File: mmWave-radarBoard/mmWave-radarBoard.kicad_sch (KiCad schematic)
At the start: 1 part, among them U2 XI6432BRQAAMY

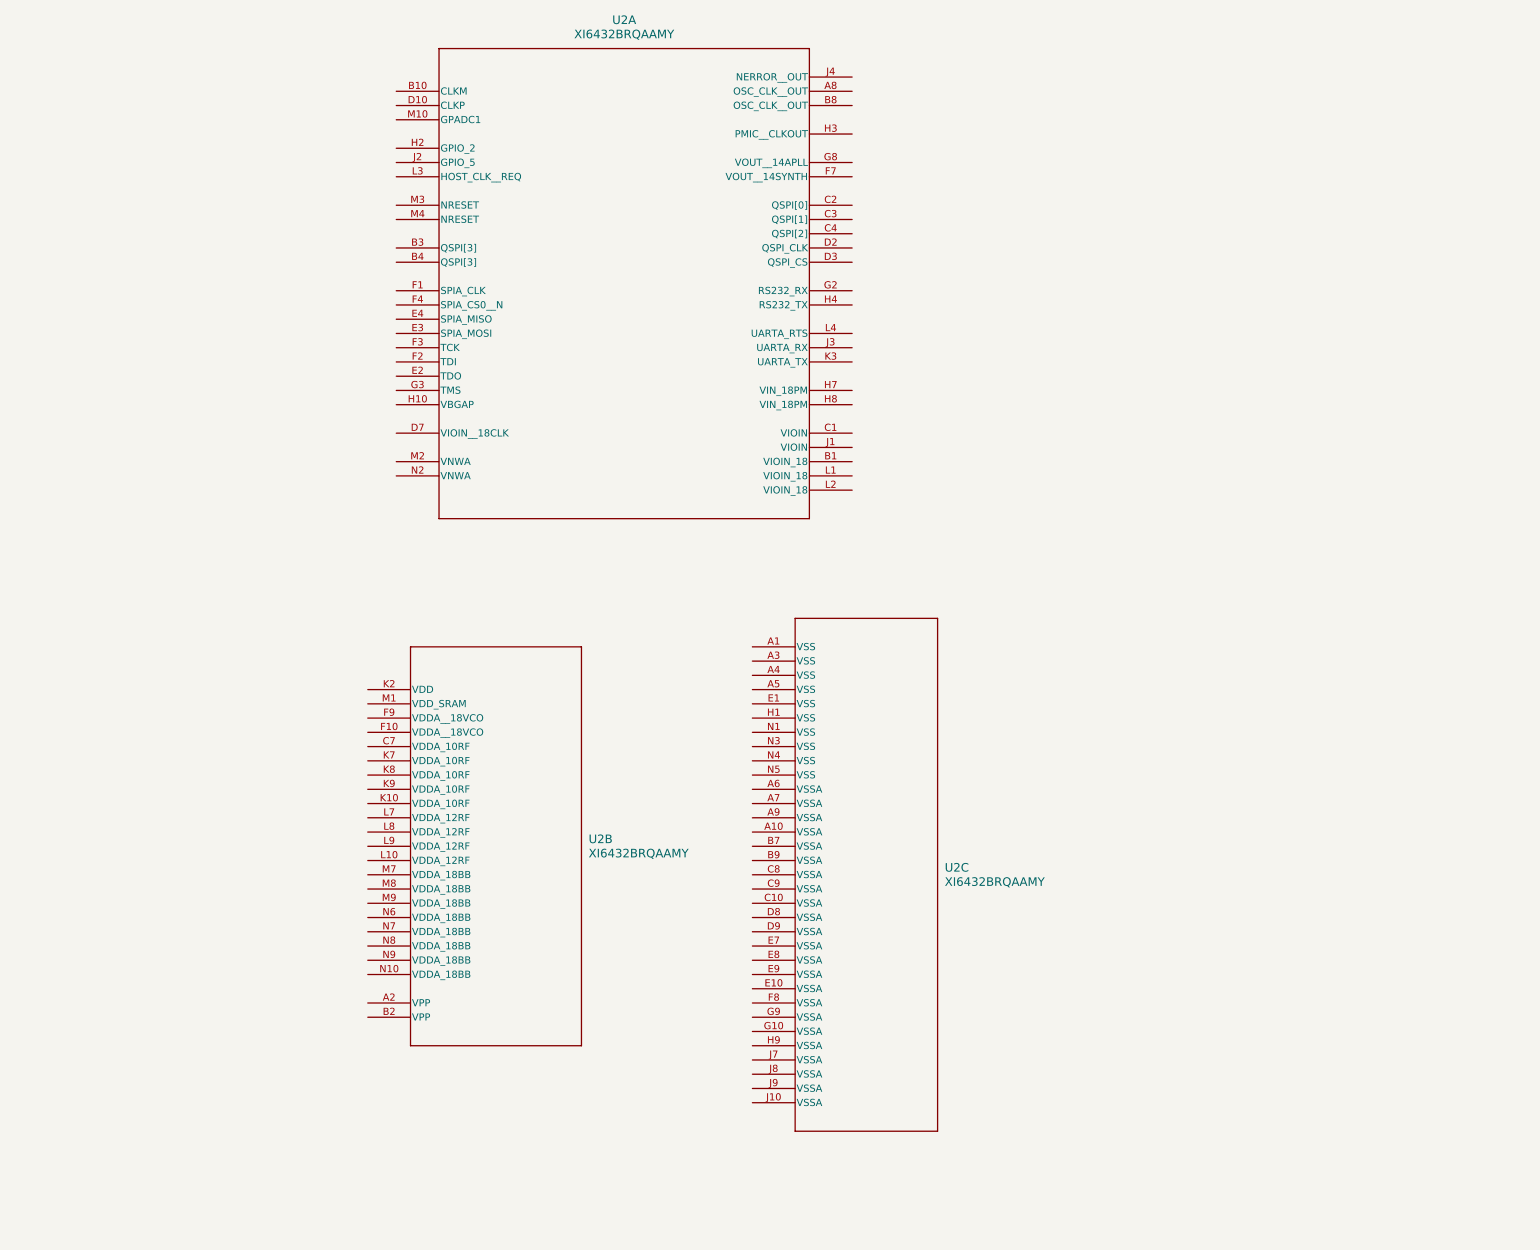
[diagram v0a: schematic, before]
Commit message: Started working on the schematic
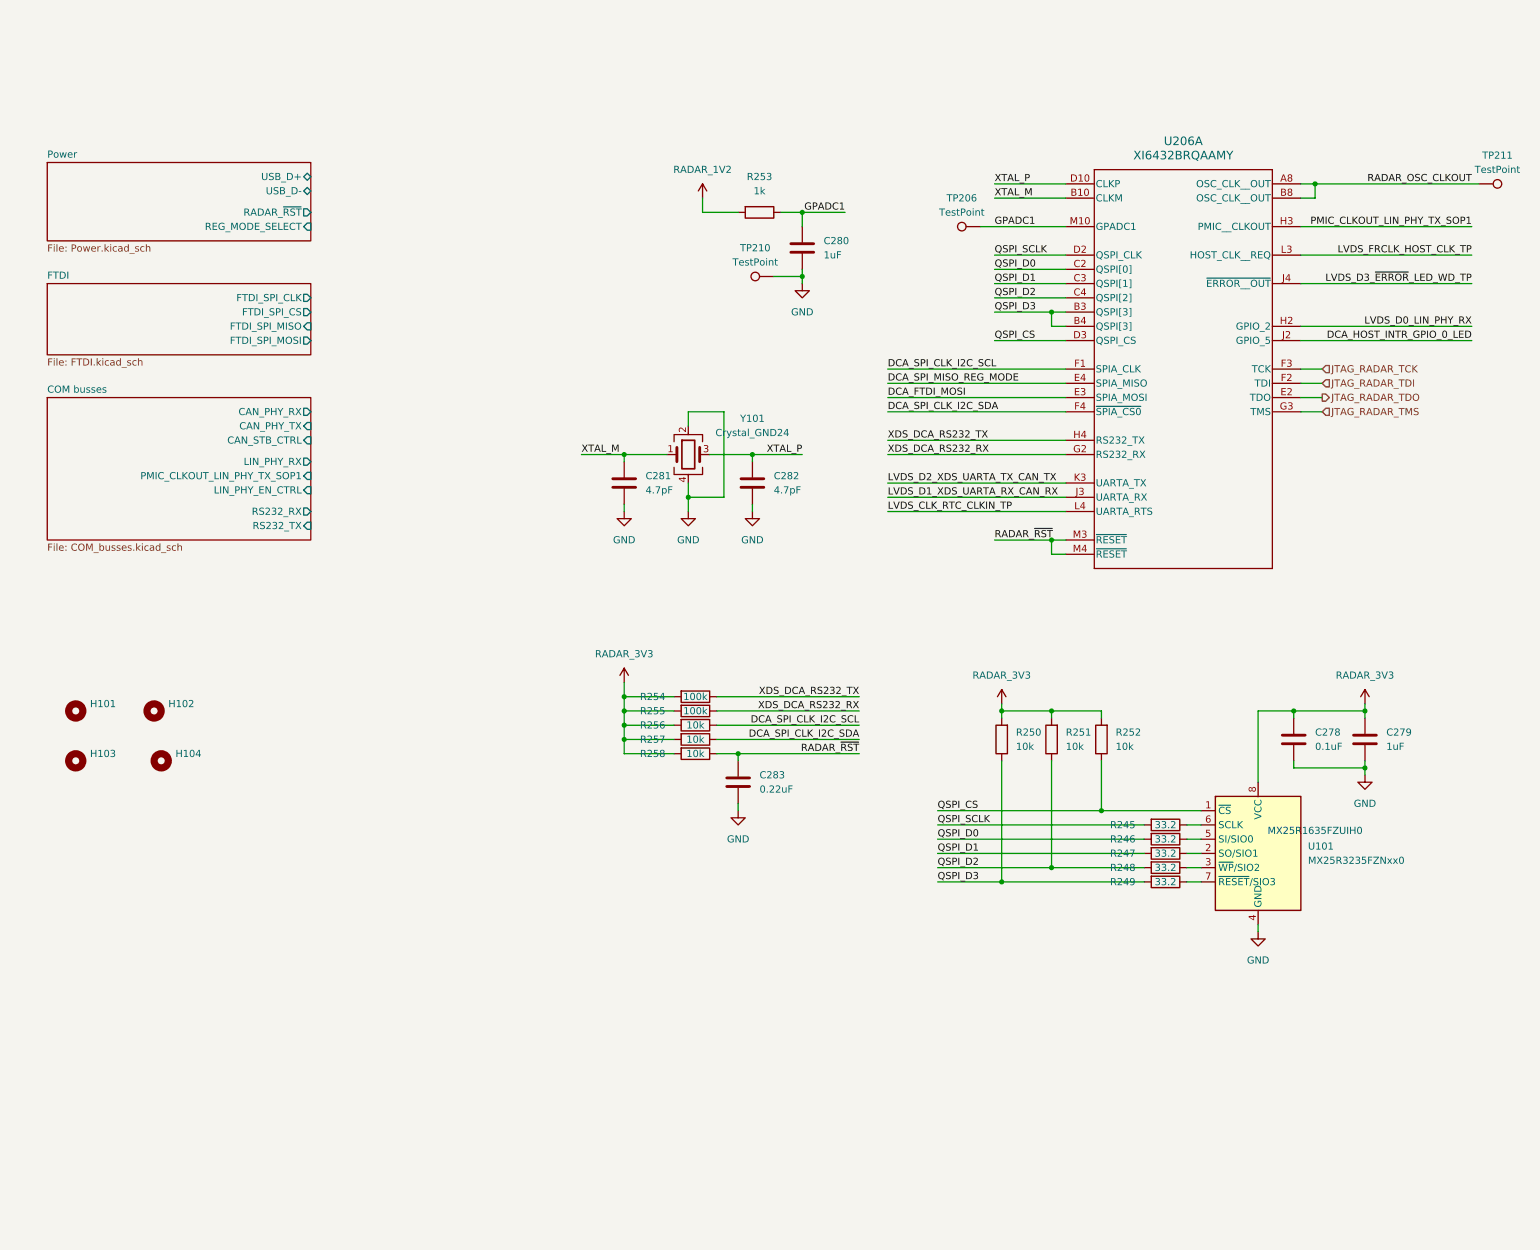
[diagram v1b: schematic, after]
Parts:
- removed U2: XI6432BRQAAMY, FCCSP101_AMY_TEX, symbol XI6432B:XI6432BRQAAMY
- added C278: 0.1uF, symbol Device:C
- added C279, C280: 1uF, symbol Device:C
- added C281, C282: 4.7pF, symbol Device:C
- added C283: 0.22uF, symbol Device:C
- added H101, H102, H103, H104: MountingHole, symbol Mechanical:MountingHole
- added R245, R246, R247, R248, R249: 33.2, symbol Device:R
- added R250, R251, R252, R256, R257, R258: 10k, symbol Device:R
- added R253: 1k, symbol Device:R
- added R254, R255: 100k, symbol Device:R
- added TP206, TP210, TP211: TestPoint, symbol Connector:TestPoint
- added U101: MX25R3235FZNxx0, Package_SON:WSON-8-1EP_6x5mm_P1.27mm_EP3.4x4mm, symbol Memory_Flash:MX25R3235FZNxx0
- added U206: XI6432BRQAAMY, FCCSP101_AMY_TEX, symbol XI6432B:XI6432BRQAAMY
- added Y101: Crystal_GND24, Crystal:Crystal_SMD_2016-4Pin_2.0x1.6mm, symbol Device:Crystal_GND24
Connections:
- new net: R249.1, U101.7 (~{RESET}/SIO3)
- new net: R245.1, U101.6 (SCLK)
- new net: R248.1, U101.3 (~{WP}/SIO2)
- new net: R247.1, U101.2 (SO/SIO1)
- new net: R246.1, U101.5 (SI/SIO0)
- new net DCA_FTDI_MOSI: U206.E3 (SPIA_MOSI)
- new net DCA_HOST_INTR_GPIO_0_LED: U206.J2 (GPIO_5)
- new net DCA_SPI_CLK_I2C_SCL: R256.1, U206.F1 (SPIA_CLK)
- new net DCA_SPI_CLK_I2C_SDA: R257.1, U206.F4 (~{SPIA_CS0})
- new net DCA_SPI_MISO_REG_MODE: U206.E4 (SPIA_MISO)
- new net GND: C278.2, C279.2, C280.2, C281.2, C282.2, C283.2, TP210.1, U101.4 (GND), U101.9 (GND), Y101.2, Y101.4
- new net GPADC1: C280.1, R253.1, TP206.1, U206.M10 (GPADC1)
- new net JTAG_RADAR_TCK: U206.F3 (TCK)
- new net JTAG_RADAR_TDI: U206.F2 (TDI)
- new net JTAG_RADAR_TDO: U206.E2 (TDO)
- new net JTAG_RADAR_TMS: U206.G3 (TMS)
- new net LVDS_CLK_RTC_CLKIN_TP: U206.L4 (UARTA_RTS)
- new net LVDS_D0_LIN_PHY_RX: U206.H2 (GPIO_2)
- new net LVDS_D1_XDS_UARTA_RX_CAN_RX: U206.J3 (UARTA_RX)
- new net LVDS_D2_XDS_UARTA_TX_CAN_TX: U206.K3 (UARTA_TX)
- new net LVDS_D3_~{ERROR}_LED_WD_TP: U206.J4 (~{ERROR__OUT})
- new net LVDS_FRCLK_HOST_CLK_TP: U206.L3 (HOST_CLK__REQ)
- new net PMIC_CLKOUT_LIN_PHY_TX_SOP1: U206.H3 (PMIC__CLKOUT)
- new net QSPI_CS: R252.1, U101.1 (~{CS}), U206.D3 (QSPI_CS)
- new net QSPI_D0: R246.2, U206.C2 (QSPI[0])
- new net QSPI_D1: R247.2, U206.C3 (QSPI[1])
- new net QSPI_D2: R248.2, R251.1, U206.C4 (QSPI[2])
- new net QSPI_D3: R249.2, R250.1, U206.B3 (QSPI[3]), U206.B4 (QSPI[3])
- new net QSPI_SCLK: R245.2, U206.D2 (QSPI_CLK)
- new net RADAR_1V2: R253.2
- new net RADAR_3V3: C278.1, C279.1, R250.2, R251.2, R252.2, R254.2, R255.2, R256.2, R257.2, R258.2, U101.8 (VCC)
- new net RADAR_OSC_CLKOUT: TP211.1, U206.A8 (OSC_CLK__OUT), U206.B8 (OSC_CLK__OUT)
- new net RADAR_~{RST}: C283.1, R258.1, U206.M3 (~{RESET}), U206.M4 (~{RESET})
- new net XDS_DCA_RS232_RX: R255.1, U206.G2 (RS232_RX)
- new net XDS_DCA_RS232_TX: R254.1, U206.H4 (RS232_TX)
- new net XTAL_M: C281.1, U206.B10 (CLKM), Y101.1
- new net XTAL_P: C282.1, U206.D10 (CLKP), Y101.3
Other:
- added sheet COM busses (COM_busses.kicad_sch)
- added sheet FTDI (FTDI.kicad_sch)
- added sheet Power (Power.kicad_sch)
- note added: "MX25R1635FZUIH0"
- company: (none) -> Emiel V

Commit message: Updated schematic
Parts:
- removed C278: 0.1uF, symbol Device:C
- removed C279, C280: 1uF, symbol Device:C
- removed C281, C282: 4.7pF, symbol Device:C
- removed C283: 0.22uF, symbol Device:C
- removed R245, R246, R247, R248, R249: 33.2, symbol Device:R
- removed R250, R251, R252, R256, R257, R258: 10k, symbol Device:R
- removed R253: 1k, symbol Device:R
- removed R254, R255: 100k, symbol Device:R
- removed TP206, TP210, TP211: TestPoint, symbol Connector:TestPoint
- removed U101: MX25R3235FZNxx0, Package_SON:WSON-8-1EP_6x5mm_P1.27mm_EP3.4x4mm, symbol Memory_Flash:MX25R3235FZNxx0
- removed U206: XI6432BRQAAMY, FCCSP101_AMY_TEX, symbol XI6432B:XI6432BRQAAMY
- removed Y101: Crystal_GND24, Crystal:Crystal_SMD_2016-4Pin_2.0x1.6mm, symbol Device:Crystal_GND24
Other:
- added sheet Muxes (Muxes.kicad_sch)
- added sheet User switches and reset (USR_SW-USR_RST.kicad_sch)
- added sheet xWRL6432AOP interface (xWRL6432AOP_interface.kicad_sch)
- note removed: "MX25R1635FZUIH0"
- company: Emiel V -> Designer: EV
- title: (none) -> Main
- moved on the sheet: H101, H102, H103, H104

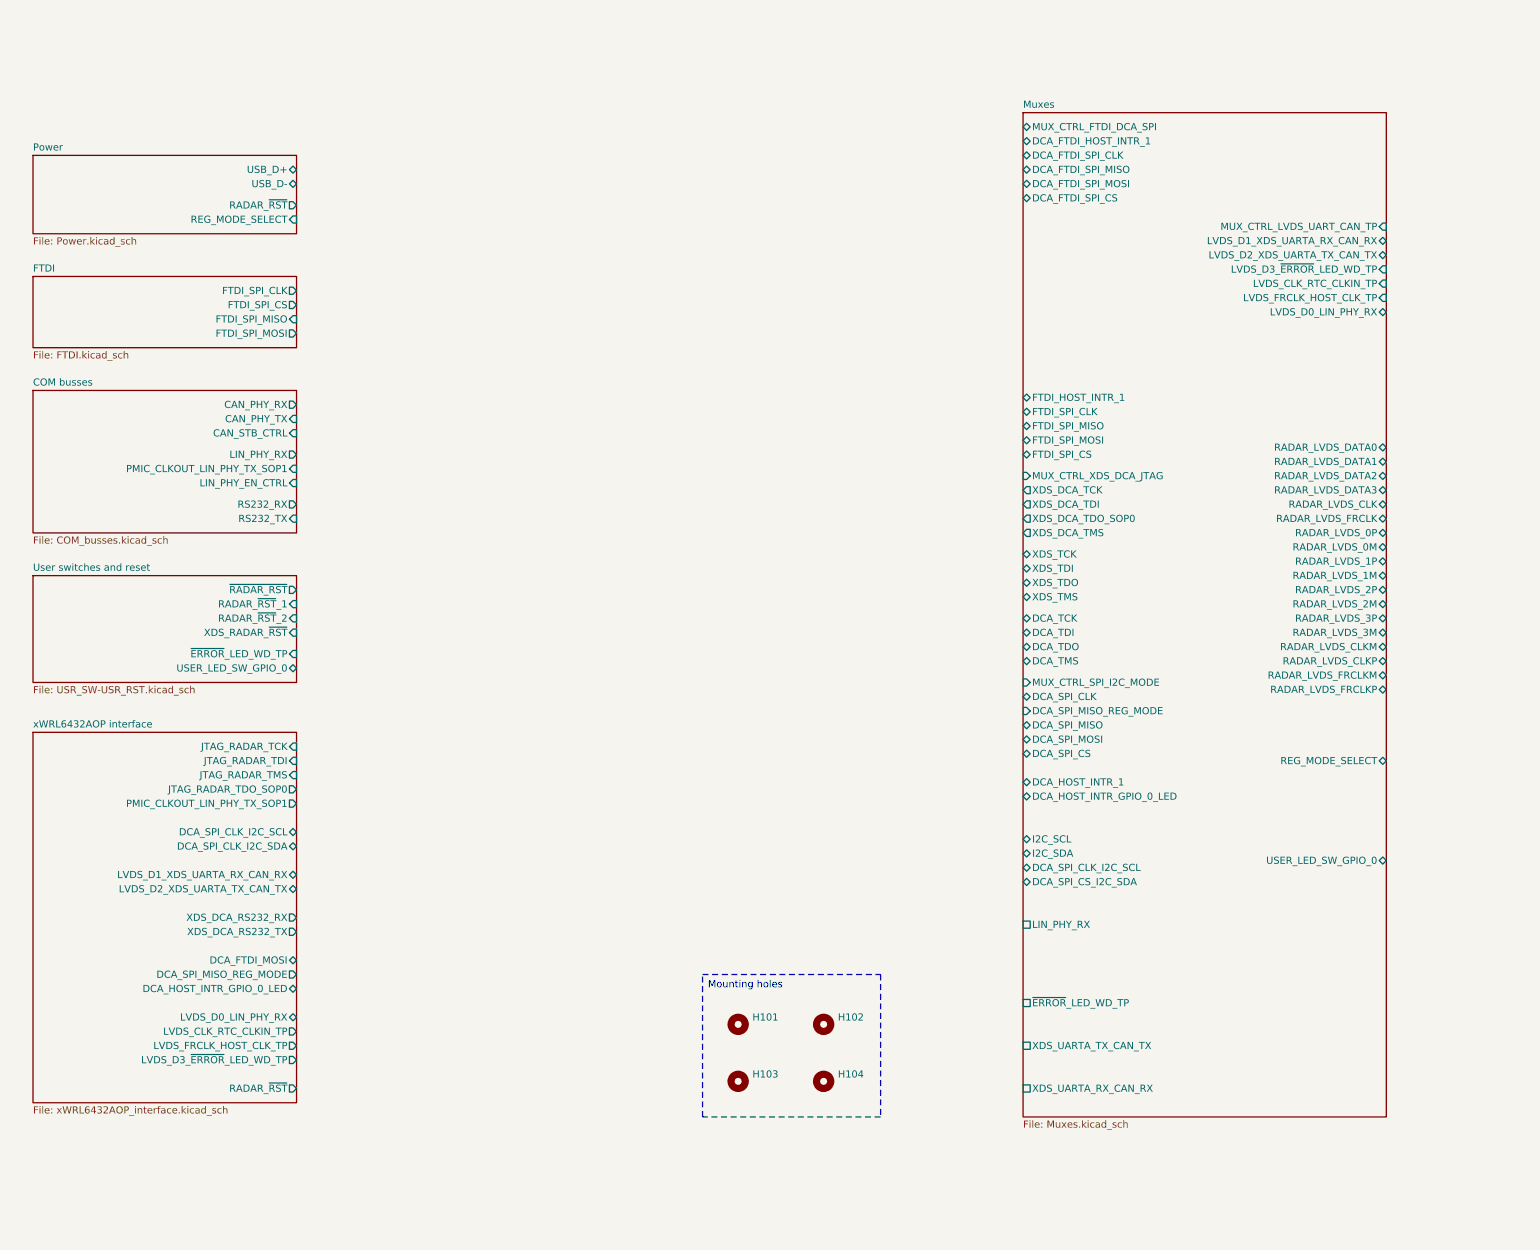
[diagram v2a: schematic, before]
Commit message: Updated schematic of the radar module
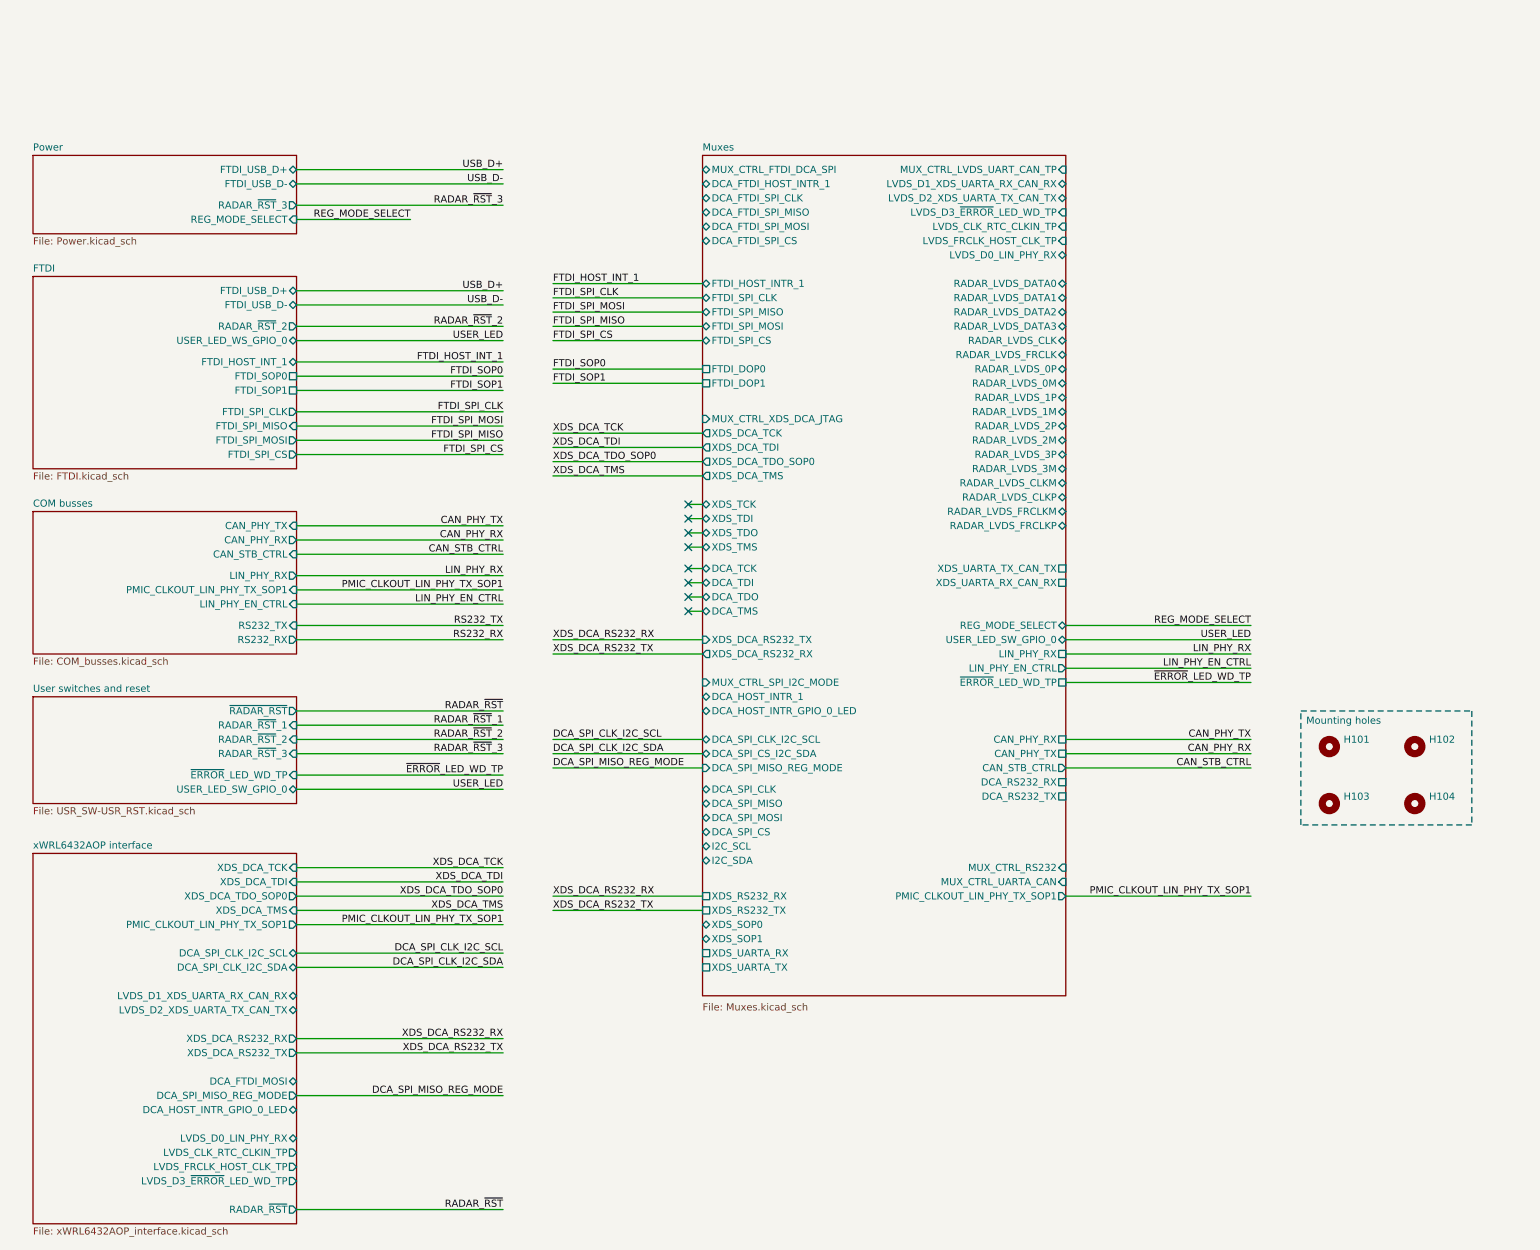
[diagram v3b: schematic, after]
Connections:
- no-connect marks 0 -> 8
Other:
- sheet FTDI ports: added FTDI_HOST_INT_1, FTDI_SOP0, FTDI_SOP1, FTDI_USB_D+, FTDI_USB_D-, RADAR_~{RST}_2, USER_LED_WS_GPIO_0; removed none
- sheet Muxes ports: added CAN_PHY_RX, CAN_PHY_TX, CAN_STB_CTRL, DCA_RS232_RX, DCA_RS232_TX, FTDI_DOP0, FTDI_DOP1, LIN_PHY_EN_CTRL, MUX_CTRL_RS232, MUX_CTRL_UARTA_CAN, PMIC_CLKOUT_LIN_PHY_TX_SOP1, XDS_DCA_RS232_RX, XDS_DCA_RS232_TX, XDS_RS232_RX, XDS_RS232_TX, XDS_SOP0, XDS_SOP1, XDS_UARTA_RX, XDS_UARTA_TX; removed none
- sheet Power ports: added FTDI_USB_D+, FTDI_USB_D-, RADAR_~{RST}_3; removed RADAR_~{RST}, USB_D+, USB_D-
- sheet User switches and reset ports: added RADAR_~{RST}_3; removed XDS_RADAR_~{RST}
- sheet xWRL6432AOP interface ports: added XDS_DCA_TCK, XDS_DCA_TDI, XDS_DCA_TDO_SOP0, XDS_DCA_TMS; removed JTAG_RADAR_TCK, JTAG_RADAR_TDI, JTAG_RADAR_TDO_SOP0, JTAG_RADAR_TMS
- moved on the sheet: H101, H102, H103, H104

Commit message: Removed unnecessary bits
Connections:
- no-connect marks 8 -> 0
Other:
- removed sheet User switches and reset
- sheet Muxes ports: added HOST_INTR_GPIO_0_LED, RADAR_~{RST}_1, RADAR_~{RST}_2, SPI_CLK_I2C_SCL, SPI_CS_I2C_SDA, SPI_MISO_REG_MODE, TDO_SOP0, ~{RADAR_RST}; removed CAN_PHY_RX, CAN_PHY_TX, DCA_FTDI_HOST_INTR_1, DCA_FTDI_SPI_CLK, DCA_FTDI_SPI_CS, DCA_FTDI_SPI_MISO, DCA_FTDI_SPI_MOSI, DCA_HOST_INTR_1, DCA_HOST_INTR_GPIO_0_LED, DCA_RS232_RX, DCA_RS232_TX, DCA_SPI_CLK, DCA_SPI_CLK_I2C_SCL, DCA_SPI_CS, DCA_SPI_CS_I2C_SDA, DCA_SPI_MISO, DCA_SPI_MISO_REG_MODE, DCA_SPI_MOSI, DCA_TCK, DCA_TDI, DCA_TDO, DCA_TMS, FTDI_SPI_MOSI, LIN_PHY_RX, LVDS_CLK_RTC_CLKIN_TP, LVDS_D0_LIN_PHY_RX, LVDS_D1_XDS_UARTA_RX_CAN_RX, LVDS_D2_XDS_UARTA_TX_CAN_TX, LVDS_D3_~{ERROR}_LED_WD_TP, LVDS_FRCLK_HOST_CLK_TP, MUX_CTRL_FTDI_DCA_SPI, MUX_CTRL_LVDS_UART_CAN_TP, MUX_CTRL_RS232, MUX_CTRL_SPI_I2C_MODE, MUX_CTRL_UARTA_CAN, MUX_CTRL_XDS_DCA_JTAG, RADAR_LVDS_0M, RADAR_LVDS_0P, RADAR_LVDS_1M, RADAR_LVDS_1P, RADAR_LVDS_2M, RADAR_LVDS_2P, RADAR_LVDS_3M, RADAR_LVDS_3P, RADAR_LVDS_CLK, RADAR_LVDS_CLKM, RADAR_LVDS_CLKP, RADAR_LVDS_DATA0, RADAR_LVDS_DATA1, RADAR_LVDS_DATA2, RADAR_LVDS_DATA3, RADAR_LVDS_FRCLK, RADAR_LVDS_FRCLKM, RADAR_LVDS_FRCLKP, XDS_DCA_RS232_RX, XDS_DCA_RS232_TX, XDS_DCA_TCK, XDS_DCA_TDI, XDS_DCA_TDO_SOP0, XDS_DCA_TMS, XDS_RS232_RX, XDS_RS232_TX, XDS_SOP0, XDS_SOP1, XDS_TCK, XDS_TDI, XDS_TDO, XDS_TMS, XDS_UARTA_RX, XDS_UARTA_RX_CAN_RX, XDS_UARTA_TX, XDS_UARTA_TX_CAN_TX, ~{ERROR}_LED_WD_TP
- sheet Power ports: added RADAR_~{RST}_1; removed RADAR_~{RST}_3
- sheet xWRL6432AOP interface ports: added CAN_RX, CAN_TX, FTDI_MOSI, HOST_INTR_GPIO_0_LED, LIN_PHY_RX, RS232_RX, RS232_TX, SPI_CLK_I2C_SCL, SPI_CLK_I2C_SDA, SPI_MISO_REG_MODE, TCK, TDI, TDO_SOP0, TMS; removed DCA_FTDI_MOSI, DCA_HOST_INTR_GPIO_0_LED, DCA_SPI_CLK_I2C_SCL, DCA_SPI_CLK_I2C_SDA, DCA_SPI_MISO_REG_MODE, LVDS_CLK_RTC_CLKIN_TP, LVDS_D0_LIN_PHY_RX, LVDS_D1_XDS_UARTA_RX_CAN_RX, LVDS_D2_XDS_UARTA_TX_CAN_TX, LVDS_D3_~{ERROR}_LED_WD_TP, LVDS_FRCLK_HOST_CLK_TP, XDS_DCA_RS232_RX, XDS_DCA_RS232_TX, XDS_DCA_TCK, XDS_DCA_TDI, XDS_DCA_TDO_SOP0, XDS_DCA_TMS
- moved on the sheet: H101, H102, H103, H104

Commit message: Finished schematic
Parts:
- added J101: Conn_01x03_Socket, Connector_JST:JST_ZE_B03B-ZESK-D_1x03_P1.50mm_Vertical, symbol Connector:Conn_01x03_Socket
- added J102: Conn_01x07_Socket, Connector_JST:JST_ZH_B7B-ZR_1x07_P1.50mm_Vertical, symbol Connector:Conn_01x07_Socket
- H101, H102, H103, H104: footprint (none) -> MountingHole:MountingHole_2.7mm_M2.5_DIN965_Pad; symbol Mechanical:MountingHole -> Mechanical:MountingHole_Pad
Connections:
- net FTDI_HOST_INT_1: now also J102.2 (Pin_2)
- net FTDI_SPI_CLK: now also J102.3 (Pin_3)
- net FTDI_SPI_CS: now also J102.4 (Pin_4)
- net FTDI_SPI_MISO: now also J102.5 (Pin_5)
- net FTDI_SPI_MOSI: now also J102.6 (Pin_6)
- new net GND: H101.1, H102.1, H103.1, H104.1, J101.3 (Pin_3), J102.7 (Pin_7)
- new net I2C_SCL: J101.1 (Pin_1)
- new net I2C_SDA: J101.2 (Pin_2)
- new net VCC_3V3: J102.1 (Pin_1)
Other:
- sheet xWRL6432AOP interface ports: added FTDI_SPI_MOSI, SPI_CS_I2C_SDA; removed FTDI_MOSI, SPI_CLK_I2C_SDA
